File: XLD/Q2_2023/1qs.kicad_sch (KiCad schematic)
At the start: 63 parts

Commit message: mend
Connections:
- net at TWPA?.: now also L:?.; no longer L:?. (x2)
- net at L:?.: now also Eccosorb?. (x2)
- net at Eccosorb?.: now also LPF?.; no longer L:?. (x2)
- net at TJI?.: now also L:?.; no longer L:?. (x2)
- net at L:?.: no longer TJI?.
- net at TJI?.: no longer L:?.
- net at L:?.: now also TJI?.
- net at L:?.: now also Coupler?.; no longer TJI?.
- net at Eccosorb?.: now also L:?.; no longer LPF?.
- net at L:?.: no longer Eccosorb?.
- net at L:?.: now also HEMT?. (gnd); no longer TJI?.
- new net: L:?., TWPA?. (x2)
- new net: L:?., TJI?. (x3)
- new net: Eccosorb?., LPF?.
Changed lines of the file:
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@@
       (project "Q2_2023"
         (path "/9924af8b-9fcb-4325-a1dc-18dd2c4184d7" (page "7"))
-        (path "/9924af8b-9fcb-4325-a1dc-18dd2c4184d7/cbbd5daf-170b-465d-a354-f5302933c82d" (page "6"))
+        (path "/9924af8b-9fcb-4325-a1dc-18dd2c4184d7/cbbd5daf-170b-465d-a354-f5302933c82d" (page "5"))
       )
     )

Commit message: more updates
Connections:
- net L3-10: no longer Coupler?.20dB
- net L3-16: no longer Coupler?.20dB
- net at L:?.: now also Eccosorb?. (x2)
- net at Eccosorb?.: now also LPF?.; no longer L:?. (x2)
- net at TJI?.: now also L:?.; no longer L:?. (x2)
- net at L:?.: no longer TJI?.
- net at TWPA?.: now also L:?.; no longer L:?.
- net at TJI?.: no longer L:?.
- net at L:?.: now also TJI?.
- net at L:?.: now also Coupler?.; no longer TJI?.
- net at Eccosorb?.: now also L:?.; no longer LPF?.
- net at L:?.: no longer Eccosorb?.
- net at L:?.: now also HEMT?. (gnd); no longer TJI?.
- new net: L:?., TJI?. (x3)
- new net: Eccosorb?., LPF?.
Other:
- moved on the sheet: TWPA?
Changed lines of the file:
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@@
     )
     (property "Value" "SMA-SMA" (at 113.665 228.6 0)
-      (effects (font (size 0.64 0.64)))
+      (effects (font (size 1 1)))
     )
     (property "Footprint" "" (at 113.03 228.6 0)
@@
     )
     (property "Value" "SMA-SMA" (at 254 160.02 0)
-      (effects (font (size 0.64 0.64)))
+      (effects (font (size 1 1)))
     )
     (property "Footprint" "" (at 253.365 160.02 0)
@@
     )
     (property "Value" "SMA-SMA" (at 341.63 201.295 0)
-      (effects (font (size 0.64 0.64)))
+      (effects (font (size 1 1)))
     )
     (property "Footprint" "" (at 340.995 201.295 0)
@@
     )
     (property "Value" "SMA-SMA" (at 229.87 226.06 0)
-      (effects (font (size 0.64 0.64)))
+      (effects (font (size 1 1)))
     )
     (property "Footprint" "" (at 229.235 226.06 0)
@@
     )
     (property "Value" "SMA-SMA" (at 254 198.12 0)
-      (effects (font (size 0.64 0.64)))
+      (effects (font (size 1 1)))
     )
     (property "Footprint" "" (at 253.365 198.12 0)
@@
     )
     (property "Value" "SMA-SMA_small" (at 229.87 177.165 0)
-      (effects (font (size 0.64 0.64)))
+      (effects (font (size 1 1)))
     )
     (property "Footprint" "" (at 229.235 177.165 0)
@@
     )
     (property "Value" "SMA-SMA" (at 254 128.27 0)
-      (effects (font (size 0.64 0.64)))
+      (effects (font (size 1 1)))
     )
     (property "Footprint" "" (at 253.365 128.27 0)
@@
     )
     (property "Value" "SMA-SMA" (at 229.87 198.12 0)
-      (effects (font (size 0.64 0.64)))
+      (effects (font (size 1 1)))
     )
     (property "Footprint" "" (at 229.235 198.12 0)
@@
     )
     (property "Value" "SMA-SMA" (at 229.87 160.02 0)
-      (effects (font (size 0.64 0.64)))
+      (effects (font (size 1 1)))
     )
     (property "Footprint" "" (at 229.235 160.02 0)
@@
     )
     (property "Value" "SMA-SMA" (at 89.535 233.045 0)
-      (effects (font (size 0.64 0.64)))
+      (effects (font (size 1 1)))
     )
     (property "Footprint" "" (at 88.9 233.045 0)
@@
     )
     (property "Value" "SMA-SMA" (at 137.795 228.6 0)
-      (effects (font (size 0.64 0.64)))
+      (effects (font (size 1 1)))
     )
     (property "Footprint" "" (at 137.16 228.6 0)
@@
     )
     (property "Value" "SMA-SMA_small" (at 254 177.165 0)
-      (effects (font (size 0.64 0.64)))
+      (effects (font (size 1 1)))
     )
     (property "Footprint" "" (at 253.365 177.165 0)
@@
     )
     (property "Value" "SMA-SMA" (at 52.07 326.39 0)
-      (effects (font (size 0.64 0.64)))
+      (effects (font (size 1 1)))
     )
     (property "Footprint" "" (at 52.07 325.755 0)
@@
     )
     (property "Value" "SMA-SMA" (at 254 226.06 0)
-      (effects (font (size 0.64 0.64)))
+      (effects (font (size 1 1)))
     )
     (property "Footprint" "" (at 253.365 226.06 0)
@@
     )
     (property "Value" "SMA-SMA" (at 52.07 314.325 0)
-      (effects (font (size 0.64 0.64)))
+      (effects (font (size 1 1)))
     )
     (property "Footprint" "" (at 52.07 313.69 0)

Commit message: update attenuators and pumplines
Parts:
- removed Coupler?: QMC-CRYOCOUPLER-20, symbol Quantum Computing:QMC-CRYOCOUPLER-20
- removed L:? (x3): SMA-SMA, symbol Quantum Computing:SMA-SMA
- removed L:?: SMA-SMA_small, symbol Quantum Computing:SMA-SMA_small
- removed TJI? (x2): LNF-ISISC4_12A, symbol Quantum Computing:LNF-ISISC4_12A
- removed TWPA?: SW_TWPA, symbol Quantum Computing:SW_TWPA
- added ATT1: Attenuator 0-Cryo, symbol Quantum Computing:Attenuator 0-Cryo
- added ATT4: Attenuator 1-Cryo, symbol Quantum Computing:Attenuator 0-Cryo
- added ATT6: Attenuator 20-Cryo, symbol Quantum Computing:Attenuator 20-Cryo
- added ATT7: Attenuator 6-Cryo, symbol Quantum Computing:Attenuator 6-Cryo
- added ATT8: Attenuator 10-Cryo, symbol Quantum Computing:Attenuator 3-Cryo
- added L:1, L:140, L:141, L:194: SMA-SMA, symbol Quantum Computing:SMA-SMA
- added L:139, L:6: COAX-6FT, symbol Quantum Computing:COAX-6FT
- added LO9: LO_R&S, symbol Quantum Computing:LO_R&S
- added LX-X2: NbTi-RF-line, symbol Quantum Computing:NbTi-RF-line
- added TJI11: LNF-ISISC4_12A, symbol Quantum Computing:LNF-ISISC4_12A
- gave numbers to parts that had none: 50
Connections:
- net L1-1: now also L:135., L:194.
- net L1-2: now also L:137.
- net L2-17: now also L:139., L:140., L:141., TJI11.
- net L3-10: now also ATT1., ATT4., ATT6., ATT7., ATT8., L:1., L:6., LO9., LX-X2.
- net at TWPA1.: now also L:132.
- net at L:133.: now also Coupler1.; no longer TWPA1.
- net at L:177.: now also Eccosorb88.
- net at Eccosorb88.: now also LPF79.; no longer L:177.
- net at TJI8.: now also L:134.; no longer L:135.
- net at Coupler1.: now also L:134.; no longer L:133.
- net at Eccosorb87.: now also L:175.; no longer LPF78.
- net at L:175.: no longer Eccosorb87.
- net at L:179.: now also Eccosorb89.
- net at Eccosorb89.: now also LPF80.; no longer L:179.
- net at Coupler1.20dB: now also L:1.
- new net: L:133., TWPA1.
- new net: L:140., TJI11.
- new net: L:135., TJI8.
- new net: L:194., TJI7.
- new net: L:6., LX-X2.
- new net: Eccosorb87., LPF78.
- new net: L:137., TJI10.
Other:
- sheet qblox_cluster_192_168_0_20 ports: added none; removed Cluster_ETH
- note added: "100mK"
- note added: "192.168.0.?"
- note added: "1K"
- note added: "20mK"
- note added: "300K"
- note added: "4K"
- note added: "50K"
- note added: "D004_200nm"
- note added: "D011_200nm"
- note removed: "D003_250nm"
- note removed: "ISOLATOR-4"
- note removed: "ISOLATOR-6"
- note removed: "ISOLATOR-7"
- note removed: "OS2"
- note removed: "OUT"
- note removed: "bottom"
- moved on the sheet: ATT293, ATT294, ATT393, ATT394, ATT395, ATT396, ATT397, ATT398, ATT399, ATT400, ATT401, ATT412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

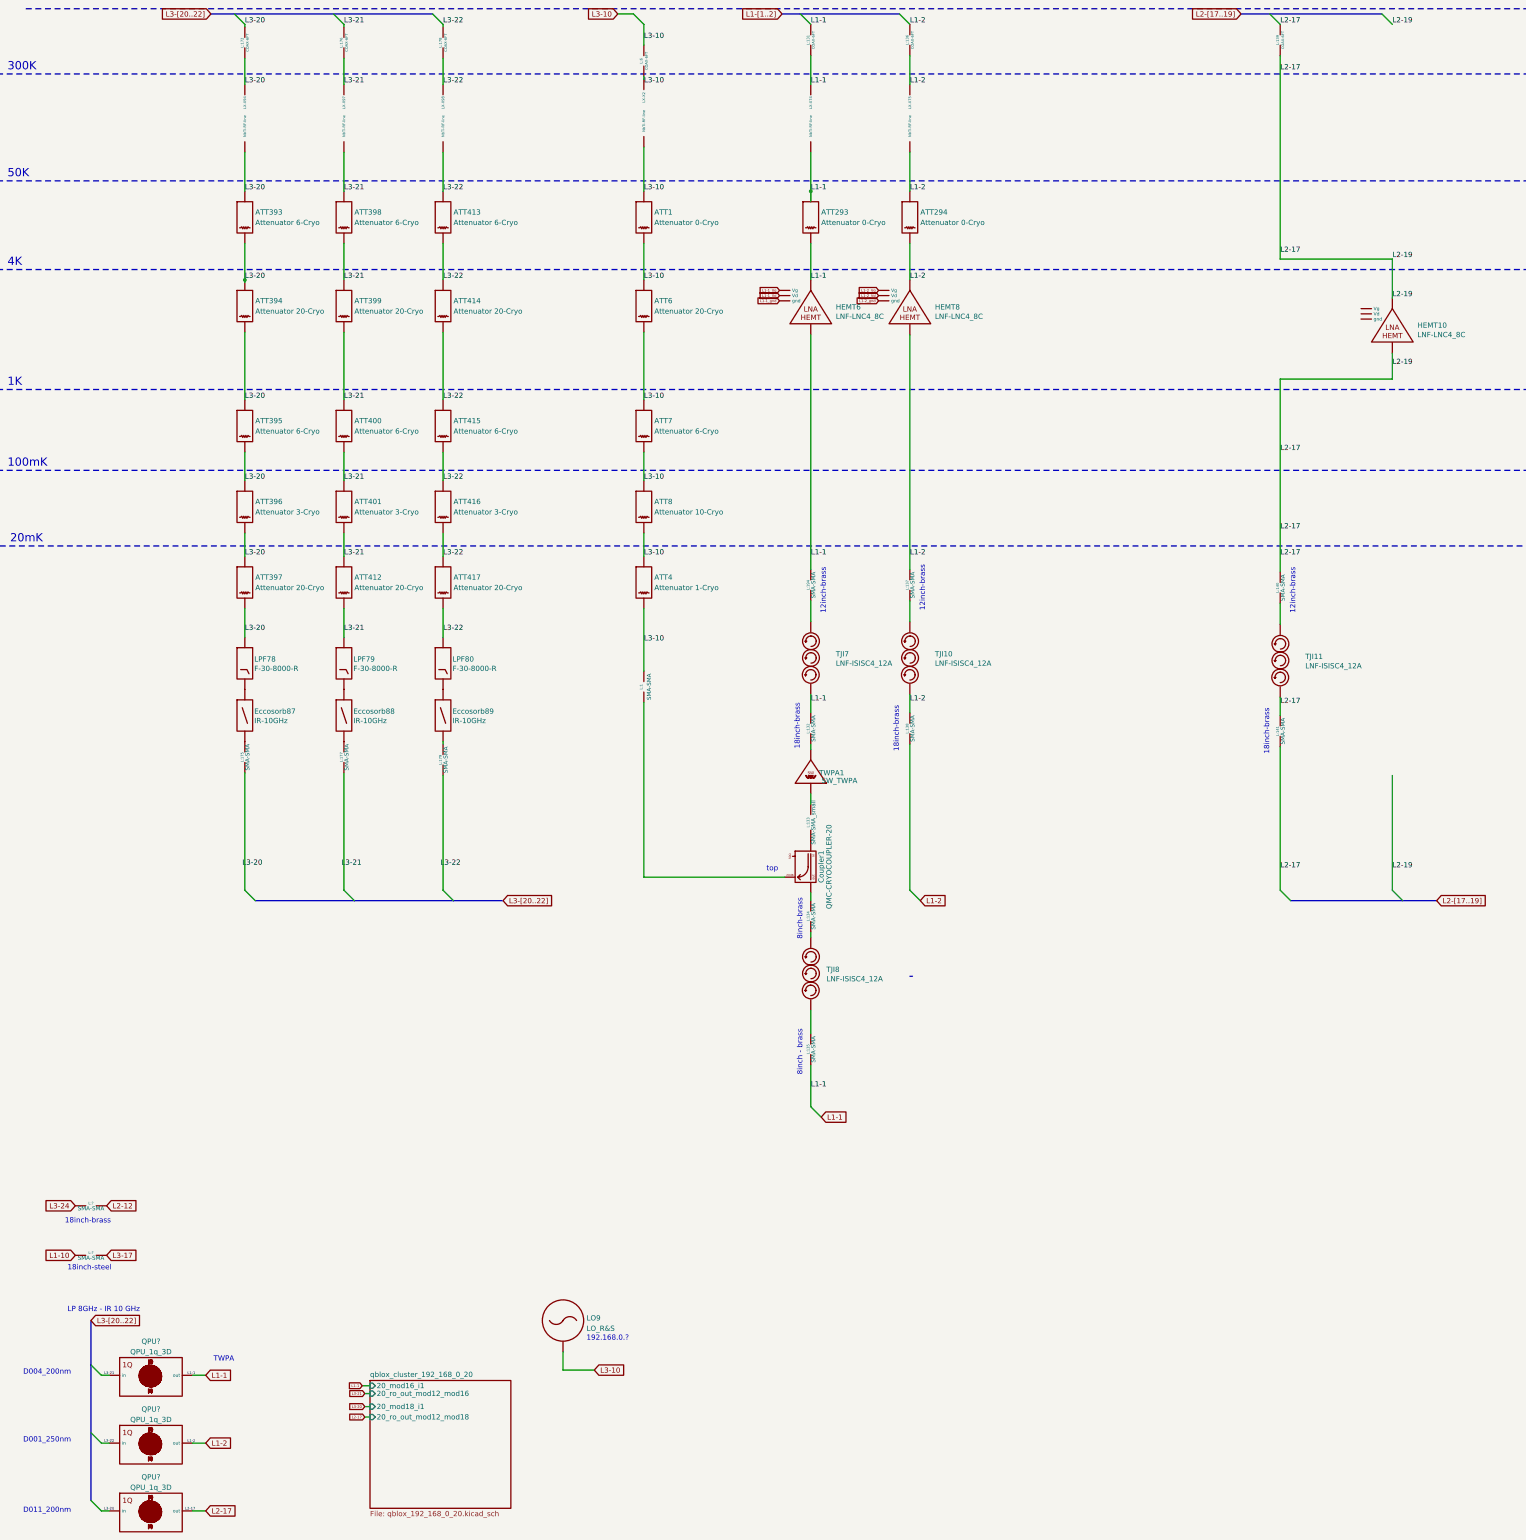
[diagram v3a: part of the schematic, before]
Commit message: Improvements to library components, title, date
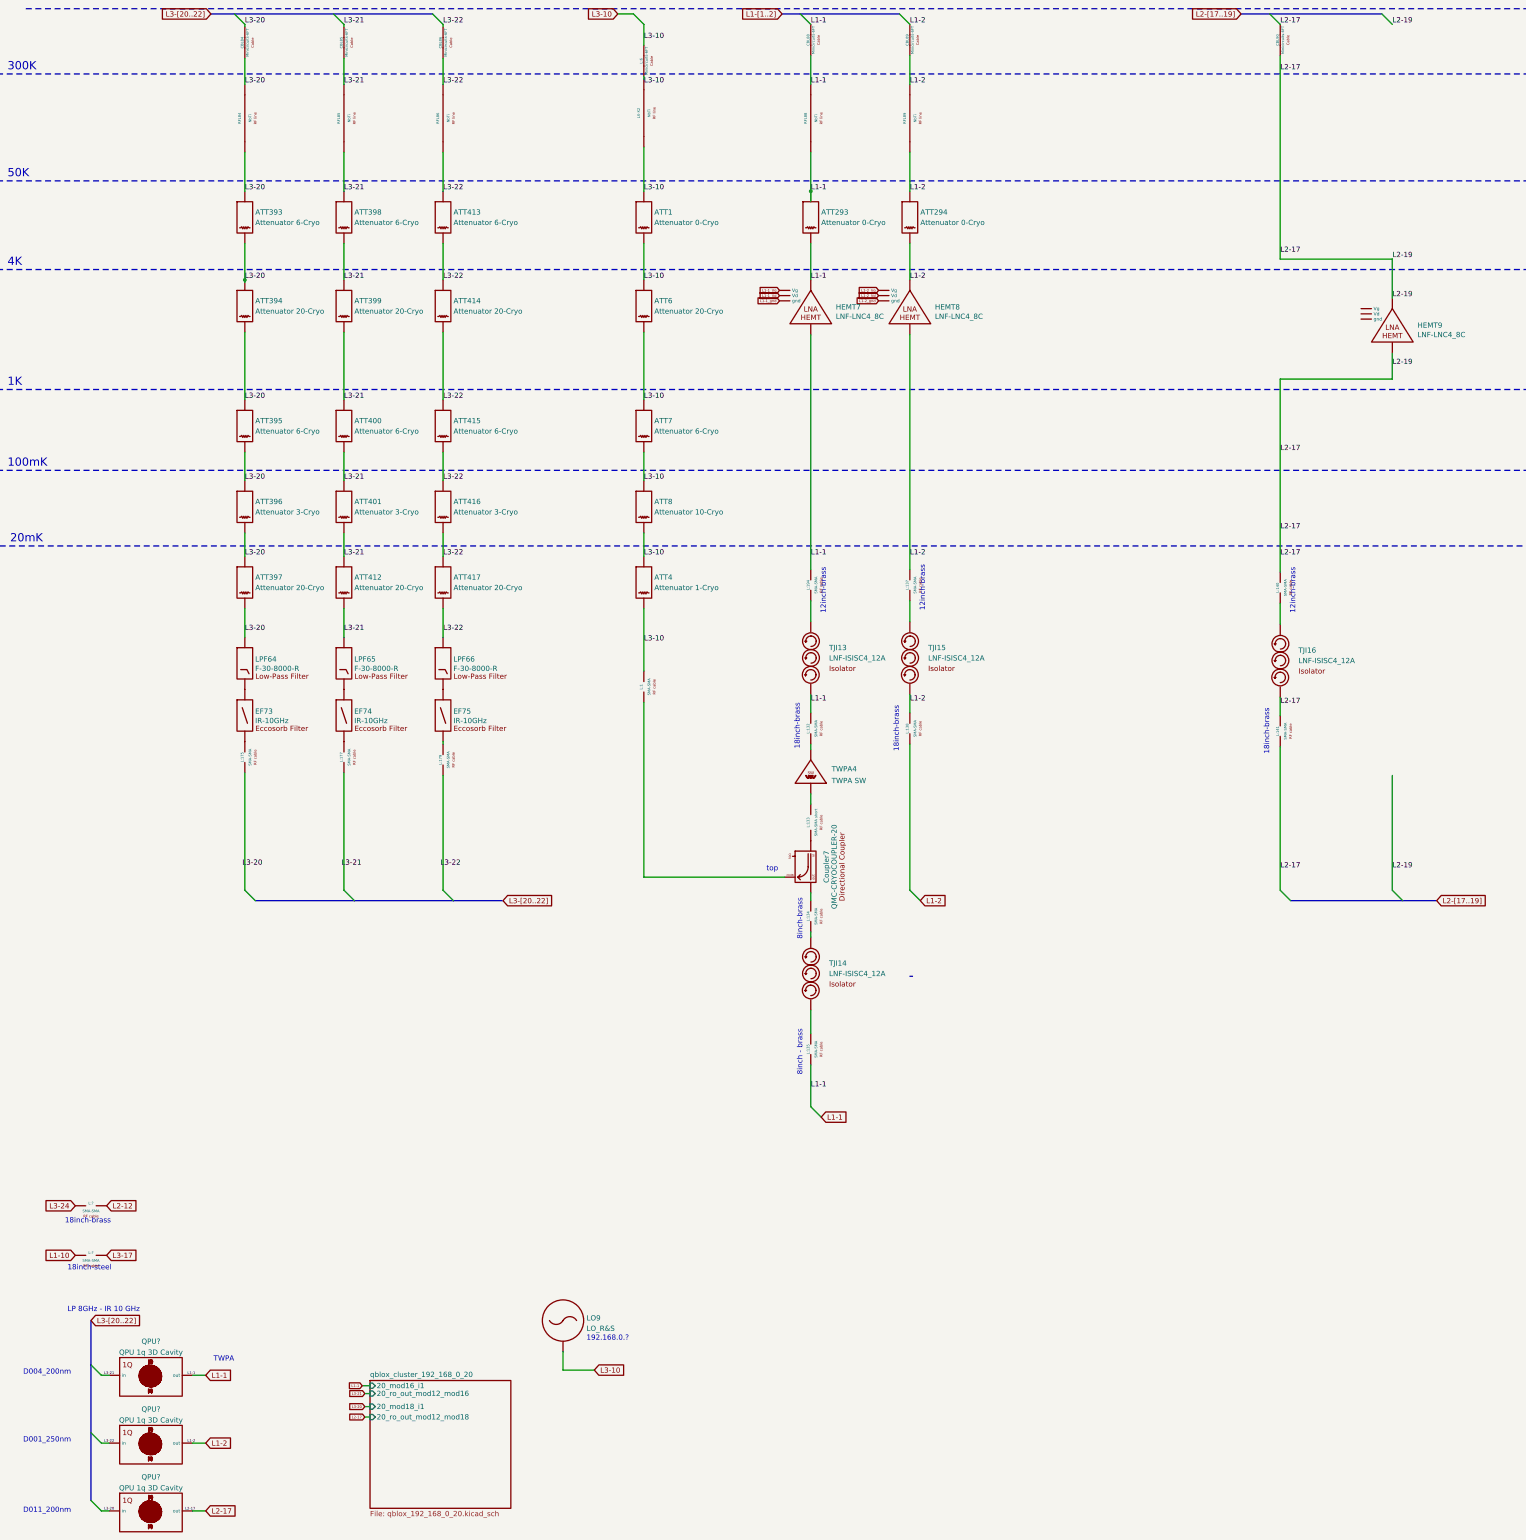
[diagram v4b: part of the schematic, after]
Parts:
- ATT4: symbol Quantum Computing:Attenuator 0-Cryo -> Quantum Computing:Attenuator 1-Cryo
- ATT8: symbol Quantum Computing:Attenuator 3-Cryo -> Quantum Computing:Attenuator 10-Cryo
- CBL84: renamed from L:172; value COAX-6FT -> Minicircuits-6FT; symbol Quantum Computing:COAX-6FT -> Quantum Computing:RF Cable Minicircuits-6FT
- CBL85: renamed from L:176; value COAX-6FT -> Minicircuits-6FT; symbol Quantum Computing:COAX-6FT -> Quantum Computing:RF Cable Minicircuits-6FT
- CBL86: renamed from L:178; value COAX-6FT -> Minicircuits-6FT; symbol Quantum Computing:COAX-6FT -> Quantum Computing:RF Cable Minicircuits-6FT
- CBL88: renamed from L:131; value COAX-6FT -> Minicircuits-6FT; symbol Quantum Computing:COAX-6FT -> Quantum Computing:RF Cable Minicircuits-6FT
- CBL89: renamed from L:136; value COAX-6FT -> Minicircuits-6FT; symbol Quantum Computing:COAX-6FT -> Quantum Computing:RF Cable Minicircuits-6FT
- CBL90: renamed from L:139; value COAX-6FT -> Minicircuits-6FT; symbol Quantum Computing:COAX-6FT -> Quantum Computing:RF Cable Minicircuits-6FT
- Coupler7: renamed from Coupler1; symbol Quantum Computing:QMC-CRYOCOUPLER-20 -> Quantum Computing:Directional Coupler QMC-CRYOCOUPLER-20
- EF73: renamed from Eccosorb87; symbol Quantum Computing:IR-10GHz -> Quantum Computing:Filter Eccosorb IR-10GHz
- EF74: renamed from Eccosorb88; symbol Quantum Computing:IR-10GHz -> Quantum Computing:Filter Eccosorb IR-10GHz
- EF75: renamed from Eccosorb89; symbol Quantum Computing:IR-10GHz -> Quantum Computing:Filter Eccosorb IR-10GHz
- HEMT7: renamed from HEMT6; symbol Quantum Computing:LNF-LNC4_8C -> Quantum Computing:Amplifier HEMT LNF-LNC4_8C
- HEMT8: symbol Quantum Computing:LNF-LNC4_8C -> Quantum Computing:Amplifier HEMT LNF-LNC4_8C
- HEMT9: renamed from HEMT10; symbol Quantum Computing:LNF-LNC4_8C -> Quantum Computing:Amplifier HEMT LNF-LNC4_8C
- L:1, L:132, L:134, L:135, L:137, L:138, L:140, L:141, L:175, L:177, L:179, L:194, L:? (x2): symbol Quantum Computing:SMA-SMA -> Quantum Computing:RF Cable SMA-SMA
- L:133: value SMA-SMA_small -> SMA-SMA short; symbol Quantum Computing:SMA-SMA_small -> Quantum Computing:RF Cable SMA-SMA_short
- L:6: value COAX-6FT -> Minicircuits-6FT; symbol Quantum Computing:COAX-6FT -> Quantum Computing:RF Cable Minicircuits-6FT
- LPF64: renamed from LPF78; symbol Quantum Computing:F-30-8000-R -> Quantum Computing:Filter Low-Pass F-30-8000-R
- LPF65: renamed from LPF79; symbol Quantum Computing:F-30-8000-R -> Quantum Computing:Filter Low-Pass F-30-8000-R
- LPF66: renamed from LPF80; symbol Quantum Computing:F-30-8000-R -> Quantum Computing:Filter Low-Pass F-30-8000-R
- LX-X2: value NbTi-RF-line -> NbTi; symbol Quantum Computing:NbTi-RF-line -> Quantum Computing:RF Line NbTi
- QPU? (x3): value QPU_1q_3D -> QPU 1q 3D Cavity; symbol Quantum Computing:QPU_1q_3D -> Quantum Computing:QPU 1q 3D Cavity
- RFL84: renamed from LX-X94; value NbTi-RF-line -> NbTi; symbol Quantum Computing:NbTi-RF-line -> Quantum Computing:RF Line NbTi
- RFL85: renamed from LX-X97; value NbTi-RF-line -> NbTi; symbol Quantum Computing:NbTi-RF-line -> Quantum Computing:RF Line NbTi
- RFL86: renamed from LX-X98; value NbTi-RF-line -> NbTi; symbol Quantum Computing:NbTi-RF-line -> Quantum Computing:RF Line NbTi
- RFL88: renamed from LX-X74; value NbTi-RF-line -> NbTi; symbol Quantum Computing:NbTi-RF-line -> Quantum Computing:RF Line NbTi
- RFL89: renamed from LX-X75; value NbTi-RF-line -> NbTi; symbol Quantum Computing:NbTi-RF-line -> Quantum Computing:RF Line NbTi
- TJI13: renamed from TJI7; symbol Quantum Computing:LNF-ISISC4_12A -> Quantum Computing:Isolator LNF-ISISC4_12A
- TJI14: renamed from TJI8; symbol Quantum Computing:LNF-ISISC4_12A -> Quantum Computing:Isolator LNF-ISISC4_12A
- TJI15: renamed from TJI10; symbol Quantum Computing:LNF-ISISC4_12A -> Quantum Computing:Isolator LNF-ISISC4_12A
- TJI16: renamed from TJI11; symbol Quantum Computing:LNF-ISISC4_12A -> Quantum Computing:Isolator LNF-ISISC4_12A
- TWPA4: renamed from TWPA1; value SW_TWPA -> TWPA SW; symbol Quantum Computing:SW_TWPA -> Quantum Computing:TWPA SW
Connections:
- net at TWPA4.: now also L:132.; no longer L:133.
- net at L:177.: now also EF74.
- net at EF74.: now also LPF65.; no longer L:177.
- net at TJI14.: now also L:134.; no longer L:135.
- net at L:134.: now also Coupler7.; no longer TJI14.
- net at EF73.: now also L:175.; no longer LPF64.
- net at L:175.: no longer EF73.
- net at L:179.: now also EF75.
- net at EF75.: now also LPF66.; no longer L:179.
- new net: L:133., TWPA4.
- new net: L:140., TJI16.
- new net: L:135., TJI14.
- new net: L:194., TJI13.
- new net: L:6., LX-X2.
- new net: EF73., LPF64.
- new net: L:137., TJI15.
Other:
- company: (none) -> Technology Innovation Institute
- title: (none) -> XLD Setup Q2 2023

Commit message: Correction in line numbers of QW 25Q
We have checked the cables of QW 25Q by connecting the IN and OUT lines to VNA and found that there is are corrections required in the line numbers mentioned in the drawing. Below are the correction made:

QW P14 - In line L3-30 , Out line L2-1
QW P29 - In line L3-26 , Out line L2-2
QW P44 - In line L3-27 , Out line L2-3
QW P59 - In line L3-18 , Out line L2-4

The Coupler pump line L3-21 replaced with L3-29
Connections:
- net at TWPA4.: now also L:132.; no longer L:133.
- net at L:177.: now also EF74.
- net at EF74.: now also LPF65.; no longer L:177.
- net at TJI14.: now also L:134.; no longer L:135.
- net at L:134.: now also Coupler7.; no longer TJI14.
- net at EF73.: now also L:175.; no longer LPF64.
- net at L:175.: no longer EF73.
- net at L:179.: now also EF75.
- net at EF75.: now also LPF66.; no longer L:179.
- new net: L:133., TWPA4.
- new net: L:140., TJI16.
- new net: L:135., TJI14.
- new net: L:194., TJI13.
- new net: L:6., LX-X2.
- new net: EF73., LPF64.
- new net: L:137., TJI15.
